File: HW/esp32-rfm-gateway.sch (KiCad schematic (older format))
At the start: 32 parts, among them J1 ph_1x2, J2 ph_1x2, J3 ph_1x3, J30 AntSMA, J4 ph_1x4, J5 ph_1x4, J6 ph_1x3, J7 ph_1x4, J8 ph_1x4, U1 ESP-WROOM-32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

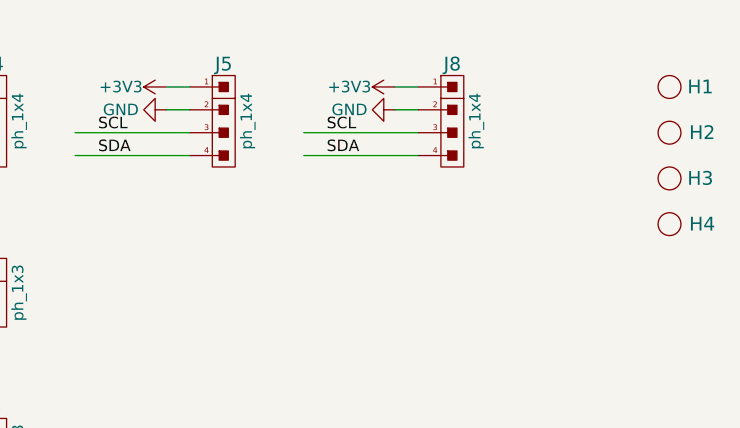
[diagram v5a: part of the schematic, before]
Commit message: Extends the I2C connector J8 to have power pins on both side for extended compatibility with other modules.
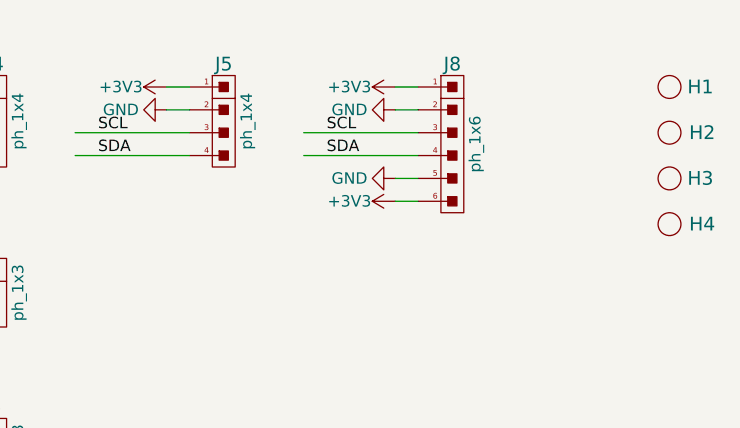
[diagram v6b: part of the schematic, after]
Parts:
- removed J8: ph_1x4, CalinConnectors:Pin_Header_Straight_1x04, symbol calin:CS_4
- added J8: ph_1x6, CalinConnectors:Pin_Header_Straight_1x06, symbol calin:CS_6
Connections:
- wire segments 142 -> 144
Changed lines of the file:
@@
 Sheet 1 3
 Title "ESP32 RFM69/RFM9x Gateway"
-Date "2019-05-03"
-Rev "36"
+Date "2019-05-04"
+Rev "37"
 Comp "Calin Radoni"
 Comment1 ""
@@
 Reset
 $Comp
-L calin:CS_4 J8
-U 1 1 5CC3F23B
-P 9300 1250
-F 0 "J8" H 9300 1500 60  0000 C CNN
-F 1 "ph_1x4" V 9400 1250 50  0000 C CNN
-F 2 "CalinConnectors:Pin_Header_Straight_1x04" H 9300 1400 60  0001 C CNN
-F 3 "" H 9300 1400 60  0000 C CNN
-	1    9300 1250
-	1    0    0    -1
-$EndComp
-$Comp
 L power:GND #PWR0178
 U 1 1 5CC3F241
@@
 Wire Wire Line
 	9900 5250 10400 5250
+$Comp
+L calin:CS_6 J8
+U 1 1 5CCEF234
+P 9300 1350
+F 0 "J8" H 9300 1700 60  0000 C CNN
+F 1 "ph_1x6" V 9400 1350 50  0000 C CNN
+F 2 "CalinConnectors:Pin_Header_Straight_1x06" H 9300 1600 60  0001 C CNN
+F 3 "" H 9300 1600 60  0000 C CNN
+F 4 "*" H 9300 1650 50  0001 C CNN "manufacturer"
+F 5 "*" H 9300 1700 50  0001 C CNN "part-number"
+F 6 "*" H 9300 1750 50  0001 C CNN "characteristics"
+F 7 "*" H 9300 1800 50  0001 C CNN "package"
+	1    9300 1350
+	1    0    0    -1
+$EndComp
+$Comp
+L power:GND #PWR0167
+U 1 1 5CCEF5ED
+P 9050 1500
+F 0 "#PWR0167" H 9050 1250 50  0001 C CNN
+F 1 "GND" V 9050 1300 50  0000 C CNN
+F 2 "" H 9050 1500 50  0000 C CNN
+F 3 "" H 9050 1500 50  0000 C CNN
+	1    9050 1500
+	0    1    1    0
+$EndComp
+$Comp
+L power:+3V3 #PWR0168
+U 1 1 5CCEF655
+P 9050 1600
+F 0 "#PWR0168" H 9050 1450 50  0001 C CNN
+F 1 "+3V3" V 9050 1800 50  0000 C CNN
+F 2 "" H 9050 1600 50  0000 C CNN
+F 3 "" H 9050 1600 50  0000 C CNN
+	1    9050 1600
+	0    -1   -1   0
+$EndComp
+Wire Wire Line
+	9050 1500 9150 1500
+Wire Wire Line
+	9150 1600 9050 1600
 $EndSCHEMATC

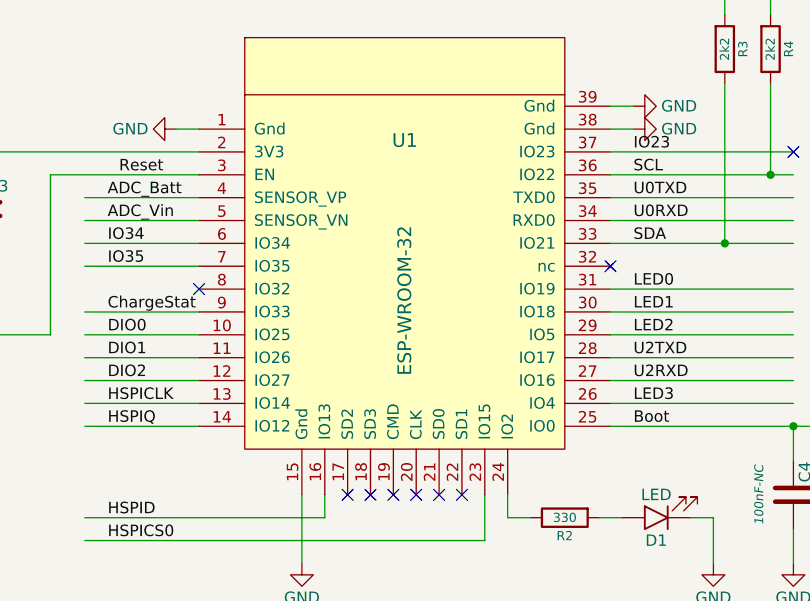
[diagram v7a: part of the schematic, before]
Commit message: Updates some part numbers.
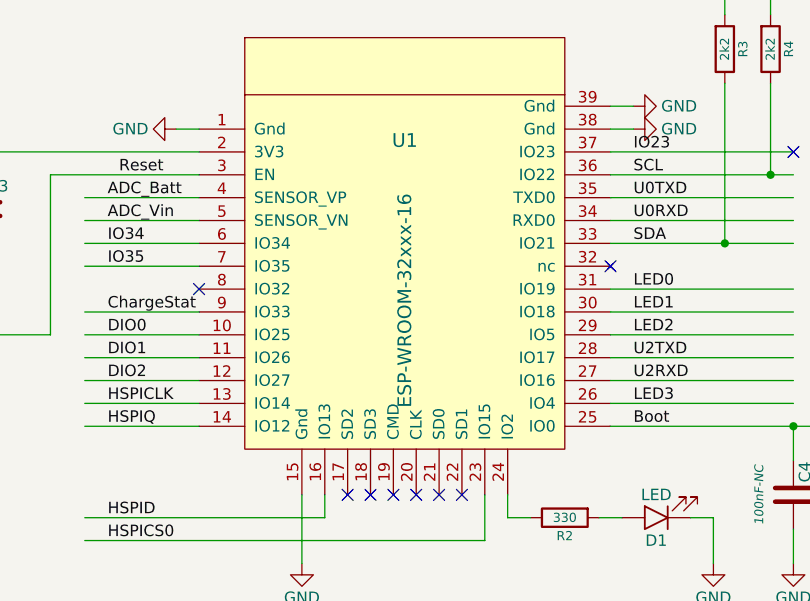
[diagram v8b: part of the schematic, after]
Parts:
- C4: Notes (none) -> DNP; Variant (none) -> DNP
- J30: characteristics (none) -> RF2-49B-T-00-50-G-HDW or RF2-03E-T-00-50-G; manufacturer (none) -> Adam Tech; part-number (none) -> RF2-49B-T-00-50-G-HDW
- R3, R4: characteristics 2k -> 2k2; part-number ERJ6ENF2001V -> ERJ-6ENF2201V
- U1: value ESP-WROOM-32 -> ESP-WROOM-32xxx-16; part-number ESP32-WROOM-32 -> ESP32-WROOM-32D-16
- U2: part-number BD49K30 -> BD48K30G-TL
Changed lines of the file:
@@
 Sheet 1 3
 Title "ESP32 RFM69/RFM9x Gateway"
-Date "2019-05-06"
+Date "2019-05-18"
 Rev "38"
 Comp "Calin Radoni"
@@
 F 6 "0805" H 0   0   50  0001 C CNN "package"
 F 7 "DNP" H 0   0   50  0001 C CNN "part-number"
+F 8 "DNP" H 0   0   50  0001 C CNN "Notes"
+F 9 "DNP" H 0   0   50  0001 C CNN "Variant"
 	1    5900 3200
 	1    0    0    -1
@@
 P 4200 2250
 F 0 "U1" H 4200 2850 60  0000 C CNN
-F 1 "ESP-WROOM-32" V 4200 2150 60  0000 C CNN
+F 1 "ESP-WROOM-32xxx-16" V 4200 2150 60  0000 C CNN
 F 2 "CalinGeneric:ESP-WROOM-32-HandSolder" H 4200 2100 60  0001 C CNN
 F 3 "" H 4200 2100 60  0001 C CNN
@@
 F 5 "Espressif" H 0   0   50  0001 C CNN "manufacturer"
 F 6 "*" H 0   0   50  0001 C CNN "package"
-F 7 "ESP32-WROOM-32" H 0   0   50  0001 C CNN "part-number"
+F 7 "ESP32-WROOM-32D-16" H 0   0   50  0001 C CNN "part-number"
 	1    4200 2250
 	1    0    0    -1
@@
 F 2 "CalinGeneric:R0805HS" V 5530 1250 30  0001 C CNN
 F 3 "" H 5600 1250 30  0000 C CNN
-F 4 "2k" H 0   0   50  0001 C CNN "characteristics"
+F 4 "2k2" H 0   0   50  0001 C CNN "characteristics"
 F 5 "Panasonic" H 0   0   50  0001 C CNN "manufacturer"
 F 6 "0805" H 0   0   50  0001 C CNN "package"
-F 7 "ERJ6ENF2001V" H 0   0   50  0001 C CNN "part-number"
+F 7 "ERJ-6ENF2201V" H 0   0   50  0001 C CNN "part-number"
 	1    5600 1250
 	1    0    0    -1
@@
 F 2 "CalinGeneric:R0805HS" V 5730 1250 30  0001 C CNN
 F 3 "" H 5800 1250 30  0000 C CNN
-F 4 "2k" H 0   0   50  0001 C CNN "characteristics"
+F 4 "2k2" H 0   0   50  0001 C CNN "characteristics"
 F 5 "Panasonic" H 0   0   50  0001 C CNN "manufacturer"
 F 6 "0805" H 0   0   50  0001 C CNN "package"
-F 7 "ERJ6ENF2001V" H 0   0   50  0001 C CNN "part-number"
+F 7 "ERJ-6ENF2201V" H 0   0   50  0001 C CNN "part-number"
 	1    5800 1250
 	1    0    0    -1
@@
 F 5 "ROHM Semiconductor" H 0   0   50  0001 C CNN "manufacturer"
 F 6 "SSOP3 (SOT23-3)" H 0   0   50  0001 C CNN "package"
-F 7 "BD49K30" H 0   0   50  0001 C CNN "part-number"
+F 7 "BD48K30G-TL" H 0   0   50  0001 C CNN "part-number"
 F 8 "DNP" H 0   0   50  0001 C CNN "Notes"
 F 9 "test" H 0   0   50  0001 C CNN "Variant"
@@
 F 2 "CalinConnectors:SMA-90" H 3250 5750 60  0001 C CNN
 F 3 "" H 3250 5750 60  0000 C CNN
+F 4 "RF2-49B-T-00-50-G-HDW or RF2-03E-T-00-50-G" H 0   0   50  0001 C CNN "characteristics"
+F 5 "Adam Tech" H 0   0   50  0001 C CNN "manufacturer"
+F 6 "RF2-49B-T-00-50-G-HDW" H 0   0   50  0001 C CNN "part-number"
 	1    3250 5550
 	1    0    0    -1
